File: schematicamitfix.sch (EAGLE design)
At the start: 39 parts, among them J1 FTDI_DEVICE, M1 WIRELESS-NRF24L01, U1 ATMEGA328P_TQFP, U2 GY-521MPU6050, U3 MAX1595EUA33+, Y1 8MHz

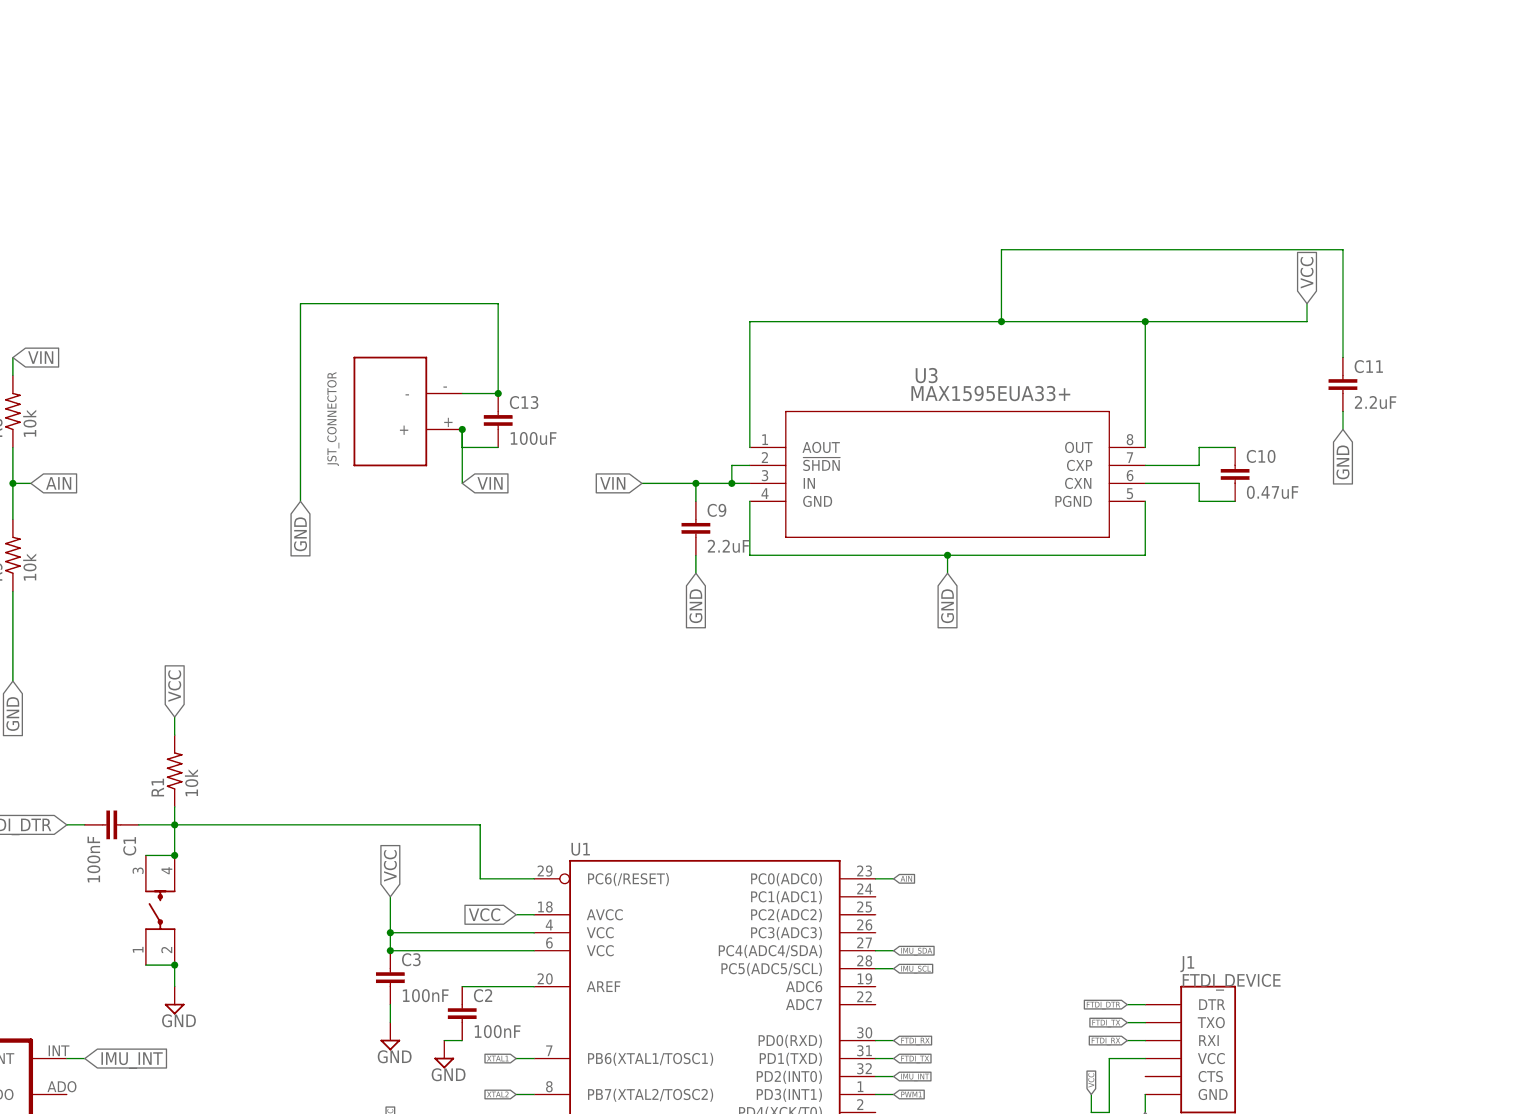
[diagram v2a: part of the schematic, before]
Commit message: Added changes to voltage regulator and cleaned up pushbutton library.
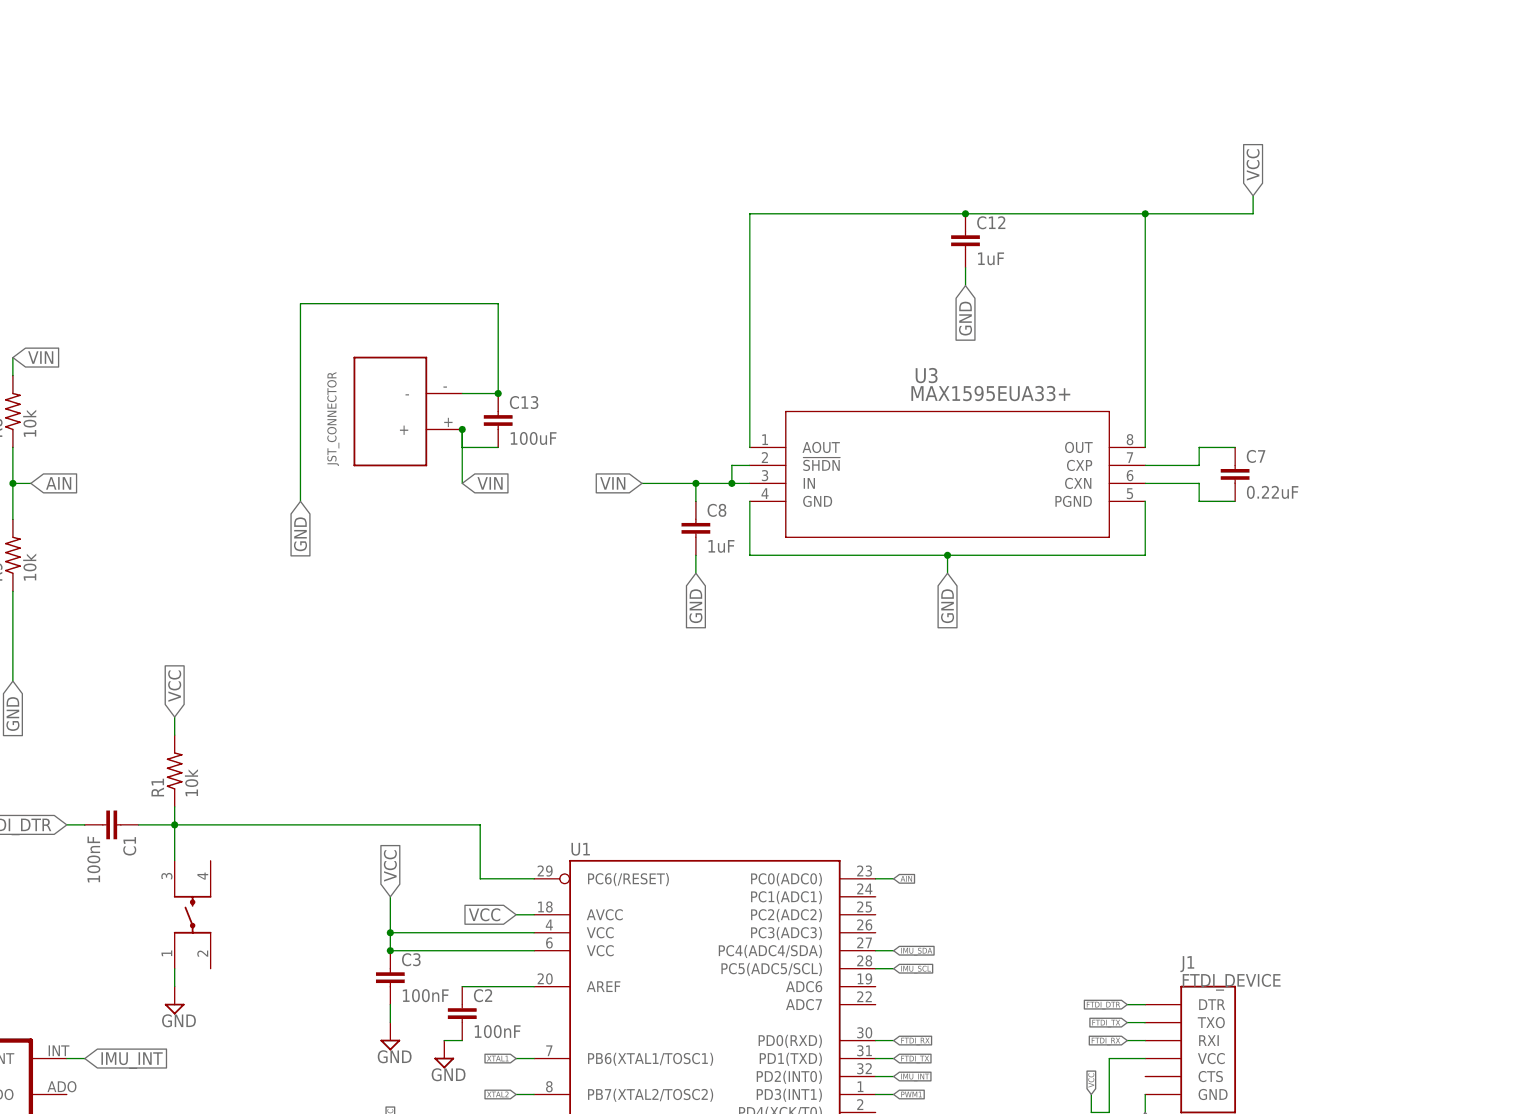
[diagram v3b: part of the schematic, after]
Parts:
- removed C11, C9: 2.2uF, rcl:C-EUC0603
- removed U$2: LL3301NF065QG, E-Switch:LL3301NF065QG
- added C12, C8: 1uF, rcl:C-EUC0805
- added U$1: LL3301NF065QG, E-Switch:LL3301NF065QG
- C7: value 0.47uF -> 0.22uF
- renumbered C10 to C7
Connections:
- net GND: now also C12.2, C8.2, U$1.1; no longer C11.2, C9.2, U$2.1, U$2.2
- net N$1: now also U$1.3; no longer U$2.3, U$2.4
- net VCC: now also C12.1; no longer C11.1
- net VIN: now also C8.1; no longer C9.1
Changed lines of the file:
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@@
 <?xml version="1.0" encoding="utf-8"?>
 <!DOCTYPE eagle SYSTEM "eagle.dtd">
-<eagle version="8.4.1">
+<eagle version="8.6.0">
 <drawing>
 <settings>
@@
 <part name="SUPPLY31" library="supply2" library_urn="urn:adsk.eagle:library:372" deviceset="GND" device=""/>
 <part name="U3" library="MAX1595EUA33+" deviceset="MAX1595EUA33+" device=""/>
-<part name="C9" library="rcl" library_urn="urn:adsk.eagle:library:334" deviceset="C-EU" device="C0603" package3d_urn="urn:adsk.eagle:package:23616/2" value="2.2uF"/>
-<part name="C10" library="rcl" library_urn="urn:adsk.eagle:library:334" deviceset="C-EU" device="C0603" package3d_urn="urn:adsk.eagle:package:23616/2" value="0.47uF"/>
-<part name="C11" library="rcl" library_urn="urn:adsk.eagle:library:334" deviceset="C-EU" device="C0603" package3d_urn="urn:adsk.eagle:package:23616/2" value="2.2uF"/>
-<part name="U$2" library="E-Switch" deviceset="LL3301NF065QG" device=""/>
 <part name="U$5" library="quad" deviceset="N-CHANNEL-MOSFET" device="-IRLML6244TRPBF"/>
 <part name="U$8" library="quad" deviceset="N-CHANNEL-MOSFET" device="-IRLML6244TRPBF"/>
@@
 <part name="SUPPLY13" library="supply2" library_urn="urn:adsk.eagle:library:372" deviceset="GND" device=""/>
 <part name="R6" library="SparkFun-Resistors" deviceset="220OHM" device="-0603-1/10W-1%" value="220"/>
+<part name="C7" library="rcl" library_urn="urn:adsk.eagle:library:334" deviceset="C-EU" device="C0603" package3d_urn="urn:adsk.eagle:package:23616/2" value="0.22uF"/>
+<part name="C8" library="rcl" library_urn="urn:adsk.eagle:library:334" deviceset="C-EU" device="C0805" package3d_urn="urn:adsk.eagle:package:23617/2" value="1uF"/>
+<part name="C12" library="rcl" library_urn="urn:adsk.eagle:library:334" deviceset="C-EU" device="C0805" package3d_urn="urn:adsk.eagle:package:23617/2" value="1uF"/>
+<part name="U$1" library="E-Switch" deviceset="LL3301NF065QG" device=""/>
 </parts>
 <sheets>
@@
 <instance part="SUPPLY31" gate="GND" x="111.76" y="-2.54"/>
 <instance part="U3" gate="A" x="66.04" y="129.54"/>
-<instance part="C9" gate="G$1" x="60.96" y="119.38"/>
-<instance part="C10" gate="G$1" x="137.16" y="127"/>
-<instance part="C11" gate="G$1" x="152.4" y="139.7"/>
-<instance part="U$2" gate="A" x="-10.16" y="68.58" rot="R90"/>
 <instance part="U$5" gate="G$1" x="246.38" y="-256.54"/>
 <instance part="U$8" gate="G$1" x="368.3" y="-134.62"/>
@@
 <instance part="SUPPLY13" gate="GND" x="-38.1" y="-30.48"/>
 <instance part="R6" gate="G$1" x="111.76" y="20.32" rot="R90"/>
+<instance part="C7" gate="G$1" x="137.16" y="127"/>
+<instance part="C8" gate="G$1" x="60.96" y="119.38"/>
+<instance part="C12" gate="G$1" x="99.06" y="160.02"/>
+<instance part="U$1" gate="A" x="-10.16" y="63.5" rot="R90"/>
 </instances>
 <busses>
@@
 </segment>
 <segment>
-<wire x1="-12.7" y1="56.388" x2="-12.7" y2="53.34" width="0.1524" layer="91"/>
-<pinref part="SUPPLY1" gate="GND" pin="GND"/>
-<pinref part="U$2" gate="A" pin="1"/>
-<wire x1="-16.764" y1="56.388" x2="-12.7" y2="56.388" width="0.1524" layer="91"/>
-<pinref part="U$2" gate="A" pin="2"/>
-<junction x="-12.7" y="56.388"/>
-</segment>
-<segment>
 <wire x1="17.78" y1="22.86" x2="17.78" y2="20.32" width="0.1524" layer="91"/>
 <pinref part="SUPPLY8" gate="GND" pin="GND"/>
@@
 <segment>
 <wire x1="60.96" y1="114.3" x2="60.96" y2="111.76" width="0.1524" layer="91"/>
-<pinref part="C9" gate="G$1" pin="2"/>
 <label x="60.96" y="111.76" size="1.778" layer="95" rot="R270" xref="yes"/>
+<pinref part="C8" gate="G$1" pin="2"/>
 </segment>
 <segment>
@@
 </segment>
 <segment>
-<pinref part="C11" gate="G$1" pin="2"/>
-<wire x1="152.4" y1="134.62" x2="152.4" y2="132.08" width="0.1524" layer="91"/>
-<label x="152.4" y="132.08" size="1.778" layer="95" rot="R270" xref="yes"/>
+<wire x1="99.06" y1="154.94" x2="99.06" y2="152.4" width="0.1524" layer="91"/>
+<label x="99.06" y="152.4" size="1.778" layer="95" rot="R270" xref="yes"/>
+<pinref part="C12" gate="G$1" pin="2"/>
 </segment>
 <segment>
@@
 <label x="124.46" y="35.56" size="0.8128" layer="95" rot="R270" xref="yes"/>
 </segment>
+<segment>
+<pinref part="SUPPLY1" gate="GND" pin="GND"/>
+<pinref part="U$1" gate="A" pin="1"/>
+<wire x1="-12.7" y1="55.88" x2="-12.7" y2="53.34" width="0.1524" layer="91"/>
+</segment>
 </net>
 <net name="IMU_INT" class="0">
@@
 </segment>
 <segment>
-<wire x1="124.46" y1="147.32" x2="147.32" y2="147.32" width="0.1524" layer="91"/>
-<wire x1="147.32" y1="147.32" x2="147.32" y2="149.86" width="0.1524" layer="91"/>
+<wire x1="124.46" y1="162.56" x2="139.7" y2="162.56" width="0.1524" layer="91"/>
+<wire x1="139.7" y1="162.56" x2="139.7" y2="165.1" width="0.1524" layer="91"/>
 <pinref part="U3" gate="A" pin="OUT"/>
-<wire x1="124.46" y1="129.54" x2="124.46" y2="147.32" width="0.1524" layer="91"/>
+<wire x1="124.46" y1="129.54" x2="124.46" y2="162.56" width="0.1524" layer="91"/>
 <pinref part="U3" gate="A" pin="AOUT"/>
-<wire x1="68.58" y1="129.54" x2="68.58" y2="147.32" width="0.1524" layer="91"/>
-<wire x1="68.58" y1="147.32" x2="104.14" y2="147.32" width="0.1524" layer="91"/>
-<junction x="124.46" y="147.32"/>
-<pinref part="C11" gate="G$1" pin="1"/>
-<wire x1="104.14" y1="147.32" x2="124.46" y2="147.32" width="0.1524" layer="91"/>
-<wire x1="152.4" y1="142.24" x2="152.4" y2="157.48" width="0.1524" layer="91"/>
-<wire x1="152.4" y1="157.48" x2="104.14" y2="157.48" width="0.1524" layer="91"/>
-<wire x1="104.14" y1="157.48" x2="104.14" y2="147.32" width="0.1524" layer="91"/>
-<junction x="104.14" y="147.32"/>
-<label x="147.32" y="149.86" size="1.778" layer="95" rot="R90" xref="yes"/>
+<wire x1="68.58" y1="129.54" x2="68.58" y2="162.56" width="0.1524" layer="91"/>
+<wire x1="68.58" y1="162.56" x2="99.06" y2="162.56" width="0.1524" layer="91"/>
+<junction x="124.46" y="162.56"/>
+<wire x1="99.06" y1="162.56" x2="124.46" y2="162.56" width="0.1524" layer="91"/>
+<junction x="99.06" y="162.56"/>
+<label x="139.7" y="165.1" size="1.778" layer="95" rot="R90" xref="yes"/>
+<pinref part="C12" gate="G$1" pin="1"/>
 </segment>
 <segment>
@@
 <wire x1="30.48" y1="76.2" x2="-12.7" y2="76.2" width="0.1524" layer="91"/>
 <junction x="-12.7" y="76.2"/>
-<wire x1="-12.7" y1="71.882" x2="-12.7" y2="76.2" width="0.1524" layer="91"/>
 <pinref part="R1" gate="G$1" pin="1"/>
 <wire x1="-12.7" y1="76.2" x2="-12.7" y2="78.74" width="0.1524" layer="91"/>
 <pinref part="C1" gate="G$1" pin="1"/>
 <wire x1="-12.7" y1="76.2" x2="-17.78" y2="76.2" width="0.1524" layer="91"/>
-<pinref part="U$2" gate="A" pin="3"/>
-<wire x1="-16.764" y1="71.882" x2="-12.7" y2="71.882" width="0.1524" layer="91"/>
 <pinref part="U1" gate="U$1" pin="PC6(/RESET)"/>
 <wire x1="38.1" y1="68.58" x2="30.48" y2="68.58" width="0.1524" layer="91"/>
 <wire x1="30.48" y1="68.58" x2="30.48" y2="76.2" width="0.1524" layer="91"/>
-<pinref part="U$2" gate="A" pin="4"/>
-<junction x="-12.7" y="71.882"/>
+<pinref part="U$1" gate="A" pin="3"/>
+<wire x1="-12.7" y1="71.12" x2="-12.7" y2="76.2" width="0.1524" layer="91"/>
 </segment>
 </net>
@@
 <junction x="60.96" y="124.46"/>
 <label x="53.34" y="124.46" size="1.778" layer="95" rot="R180" xref="yes"/>
-<pinref part="C9" gate="G$1" pin="1"/>
+<pinref part="C8" gate="G$1" pin="1"/>
 </segment>
 </net>
@@
 <wire x1="124.46" y1="127" x2="132.08" y2="127" width="0.1524" layer="91"/>
 <wire x1="132.08" y1="127" x2="132.08" y2="129.54" width="0.1524" layer="91"/>
-<pinref part="C10" gate="G$1" pin="1"/>
 <wire x1="132.08" y1="129.54" x2="137.16" y2="129.54" width="0.1524" layer="91"/>
+<pinref part="C7" gate="G$1" pin="1"/>
 </segment>
 </net>
@@
 <wire x1="132.08" y1="124.46" x2="132.08" y2="121.92" width="0.1524" layer="91"/>
 <wire x1="132.08" y1="121.92" x2="137.16" y2="121.92" width="0.1524" layer="91"/>
-<pinref part="C10" gate="G$1" pin="2"/>
-</segment>
-</net>
+<pinref part="C7" gate="G$1" pin="2"/>
+</segment>
+</net>
